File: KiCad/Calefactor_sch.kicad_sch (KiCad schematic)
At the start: 8 parts, among them K2 Relay_SPDT, Q27 AO3400A, U1 SHTC3

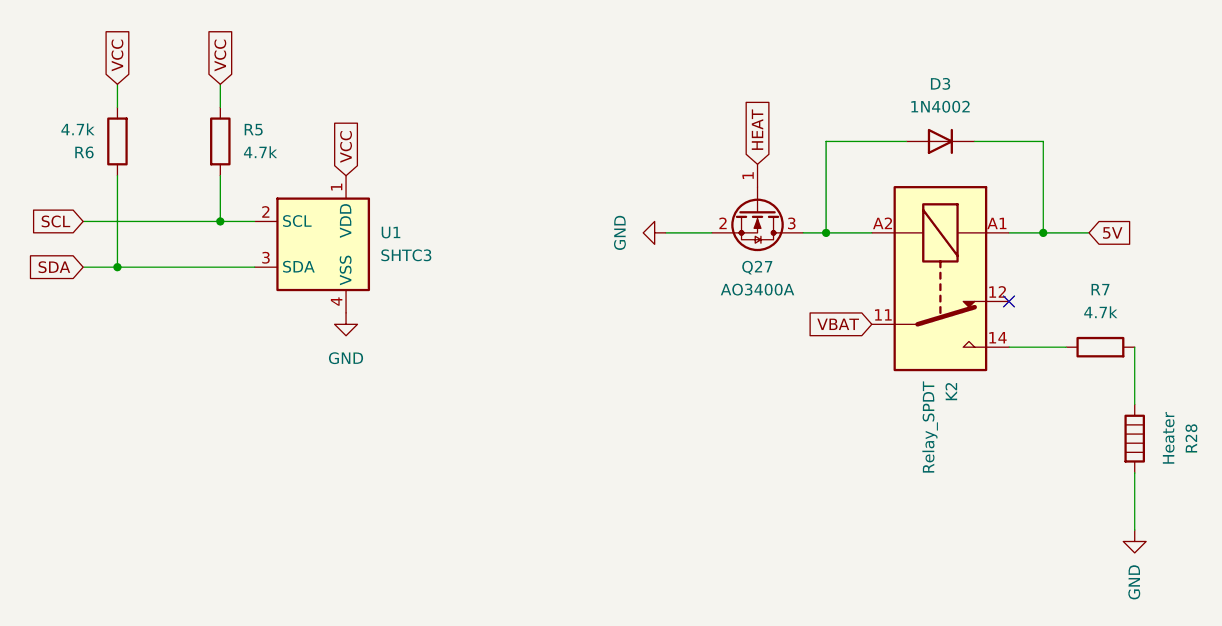
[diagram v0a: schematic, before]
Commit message: terminado placement (reorganizado pines del micro y añadido cambios de sensores/calefactor por conectores)
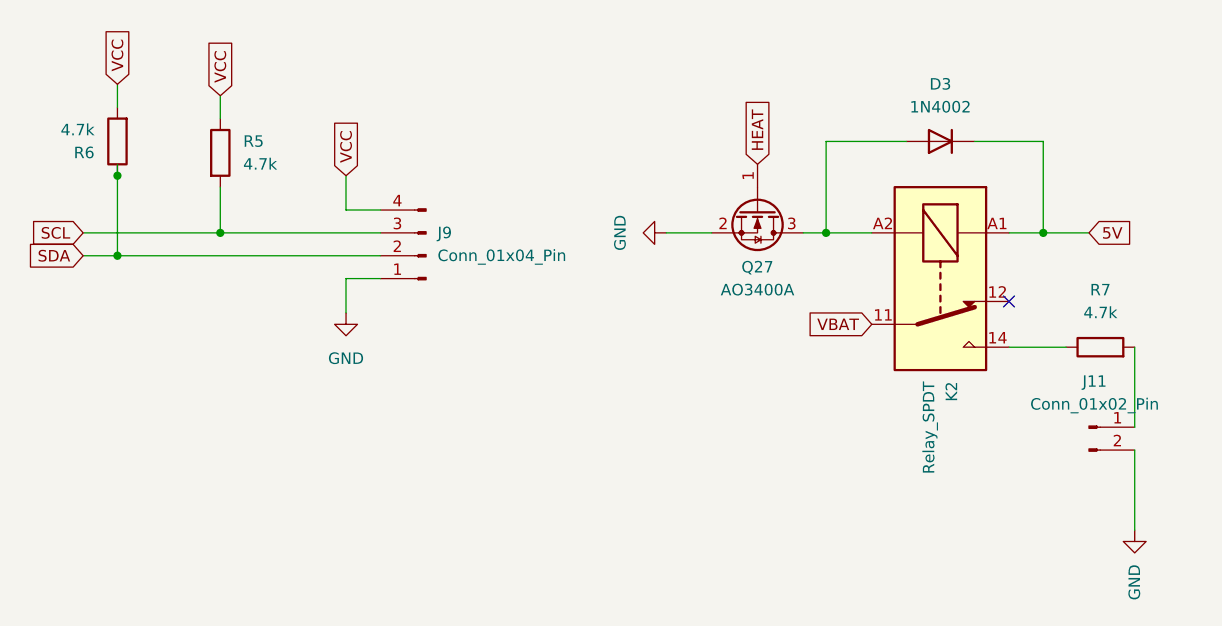
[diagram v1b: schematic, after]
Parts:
- removed R28: Heater, Resistor_THT:R_Axial_Power_L20.0mm_W6.4mm_P5.08mm_Vertical, symbol Device:Heater
- removed U1: SHTC3, Sensor_Humidity:Sensirion_DFN-4-1EP_2x2mm_P1mm_EP0.7x1.6mm, symbol Sensor_Humidity:SHTC3
- added J11: Conn_01x02_Pin, Connector_PinHeader_2.54mm:PinHeader_1x02_P2.54mm_Vertical, symbol Connector:Conn_01x02_Pin
- added J9: Conn_01x04_Pin, Connector_PinHeader_2.54mm:PinHeader_1x04_P2.54mm_Vertical, symbol Connector:Conn_01x04_Pin
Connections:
- net GND: now also J11.2 (Pin_2), J9.1 (Pin_1)
- net SCL: now also J9.3 (Pin_3)
- net SDA: now also J9.2 (Pin_2)
- net VCC: now also J9.4 (Pin_4)
- net at R7.2: now also J11.1 (Pin_1)
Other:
- moved on the sheet: R5

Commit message: versión casi final del enrutado
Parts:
- removed R7: 4.7k, Resistor_SMD:R_0603_1608Metric, symbol Device:R
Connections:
- net at K2.14: now also J11.1 (Pin_1)
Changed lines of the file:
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@@
 	(wire
 		(pts
-			(xy 181.61 83.82) (xy 187.96 83.82)
+			(xy 181.61 83.82) (xy 195.58 83.82)
 		)
 		(stroke
@@
 			)
 		)
-	)
-	(symbol
-		(lib_id "Device:R")
-		(at 191.77 83.82 90)
-		(unit 1)
-		(exclude_from_sim no)
-		(in_bom yes)
-		(on_board yes)
-		(dnp no)
-		(fields_autoplaced yes)
-		(property "Reference" "R7"
-			(at 191.77 77.47 90)
-			(effects
-				(font
-					(size 1.27 1.27)
-				)
-			)
-		)
-		(property "Value" "4.7k"
-			(at 191.77 80.01 90)
-			(effects
-				(font
-					(size 1.27 1.27)
-				)
-			)
-		)
-		(property "Footprint" "Resistor_SMD:R_0603_1608Metric"
-			(at 191.77 85.598 90)
-			(effects
-				(font
-					(size 1.27 1.27)
-				)
-				(hide yes)
-			)
-		)
-		(property "Datasheet" "~"
-			(at 191.77 83.82 0)
-			(effects
-				(font
-					(size 1.27 1.27)
-				)
-				(hide yes)
-			)
-		)
-		(property "Description" "Resistor"
-			(at 191.77 83.82 0)
-			(effects
-				(font
-					(size 1.27 1.27)
-				)
-				(hide yes)
-			)
-		)
-		(pin "2"
-		)
-		(pin "1"
-		)
-		(instances
-			(project "Retrovisores"
-				(path "/9b9f005f-0621-4675-bd4e-683e7082b120/1a76def2-ddde-4ac6-93d0-da3d16171b62"
-					(reference "R7")
-					(unit 1)
-				)
-			)
-		)

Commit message: reorganizado el esquematico
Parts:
- removed D3: 1N4002, Diode_THT:D_DO-41_SOD81_P2.54mm_Vertical_AnodeUp, symbol Diode:1N4002
- removed J11: Conn_01x02_Pin, Connector_PinHeader_2.54mm:PinHeader_1x02_P2.54mm_Vertical, symbol Connector:Conn_01x02_Pin
- removed J9: Conn_01x04_Pin, Connector_PinHeader_2.54mm:PinHeader_1x04_P2.54mm_Vertical, symbol Connector:Conn_01x04_Pin
- removed K2: Relay_SPDT, Relay_THT:Relay_1-Form-C_Schrack-RYII_RM3.2mm, symbol Relay:Relay_SPDT
- removed Q27: AO3400A, Package_TO_SOT_SMD:SOT-23, symbol Transistor_FET:AO3400A
- removed R5, R6: 4.7k, Resistor_SMD:R_0402_1005Metric, symbol Device:R
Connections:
- no-connect marks 1 -> 0
